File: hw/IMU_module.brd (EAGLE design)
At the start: 25 x 45 mm, 42 parts, among them J1 GROVE-4P-2.0-3470130P1, J2 GROVE-4P-2.0-3470130P1, X1 53047-06

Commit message: moved LSM303D interrupt lines
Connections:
- net AM_INT1: now also U$6.12; no longer U$6.11
- net AM_INT2: now also U$6.13; no longer U$6.12
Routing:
- net AM_INT2: track 4.09 -> 1.97 mm
- net AM_INT1: track 5.23 -> 3.68 mm
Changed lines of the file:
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@@
 </signal>
 <signal name="AM_INT1">
-<contactref element="U$6" pad="11"/>
 <contactref element="U$8" pad="P$11"/>
-<wire x1="18.5" y1="22.7" x2="18.5" y2="21.8" width="0.2" layer="1"/>
-<wire x1="18.5" y1="21.8" x2="19.9" y2="20.4" width="0.2" layer="1"/>
-<wire x1="19.9" y1="20.4" x2="19.9" y2="19" width="0.2" layer="1"/>
-<wire x1="19.9" y1="19" x2="19.7" y2="18.8" width="0.2" layer="1"/>
-<wire x1="19.05" y1="18.75" x2="19.65" y2="18.75" width="0.2" layer="1"/>
-<wire x1="19.65" y1="18.75" x2="19.7" y2="18.8" width="0.2" layer="1"/>
+<contactref element="U$6" pad="12"/>
+<wire x1="18.5" y1="22.7" x2="18.5" y2="21.9" width="0.2" layer="1"/>
+<wire x1="19.05" y1="19.25" x2="19.05" y2="21.35" width="0.2" layer="1"/>
+<wire x1="19.05" y1="21.35" x2="18.5" y2="21.9" width="0.2" layer="1"/>
 </signal>
 <signal name="AM_INT2">
-<contactref element="U$6" pad="12"/>
 <contactref element="U$8" pad="P$9"/>
-<wire x1="17.5" y1="22.7" x2="17.5" y2="22.2" width="0.2" layer="1"/>
-<wire x1="19.05" y1="19.25" x2="19.05" y2="20.65" width="0.2" layer="1"/>
-<wire x1="17.5" y1="22.2" x2="19.05" y2="20.65" width="0.2" layer="1"/>
+<contactref element="U$6" pad="13"/>
+<wire x1="17.55" y1="20.75" x2="17.55" y2="21.85" width="0.2" layer="1"/>
+<wire x1="17.55" y1="21.85" x2="17.5" y2="21.9" width="0.2" layer="1"/>
+<wire x1="17.5" y1="21.9" x2="17.5" y2="22.7" width="0.2" layer="1"/>
 </signal>
 <signal name="BAR_CS">

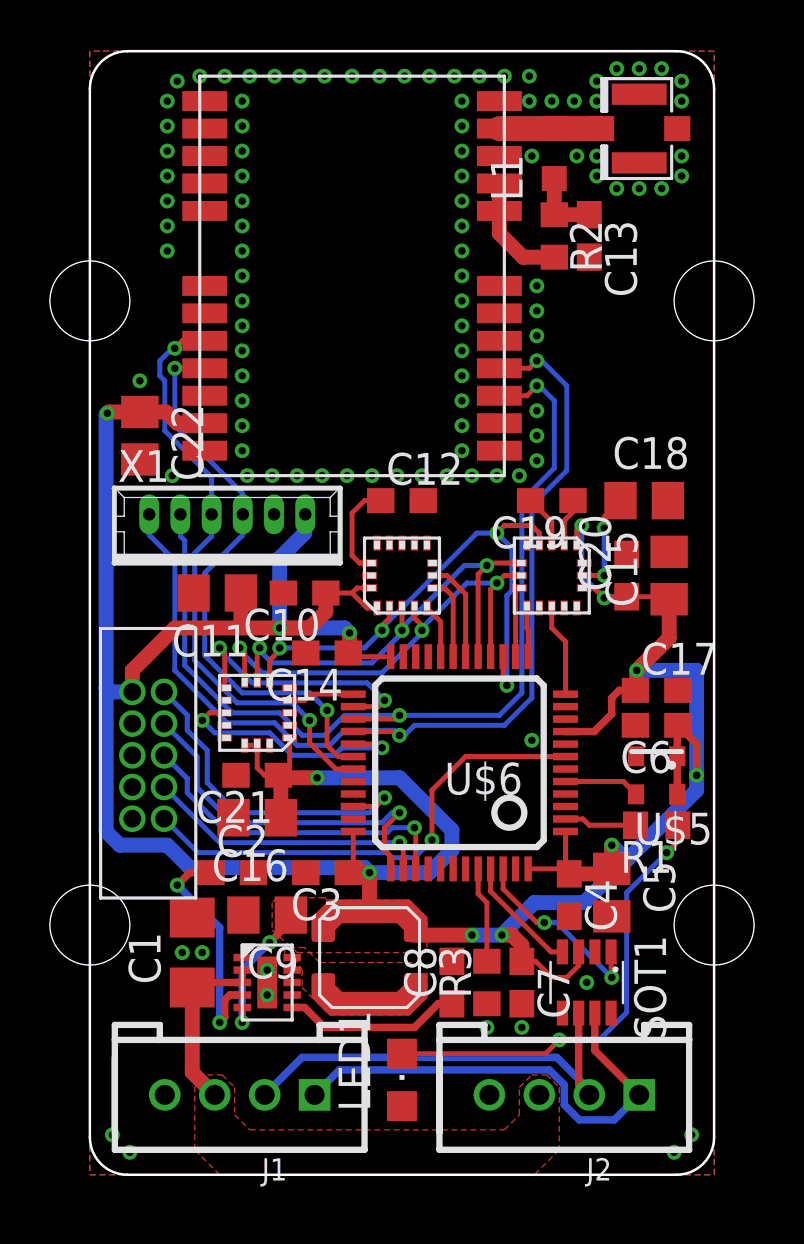
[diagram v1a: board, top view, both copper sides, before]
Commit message: approved DRC false errors
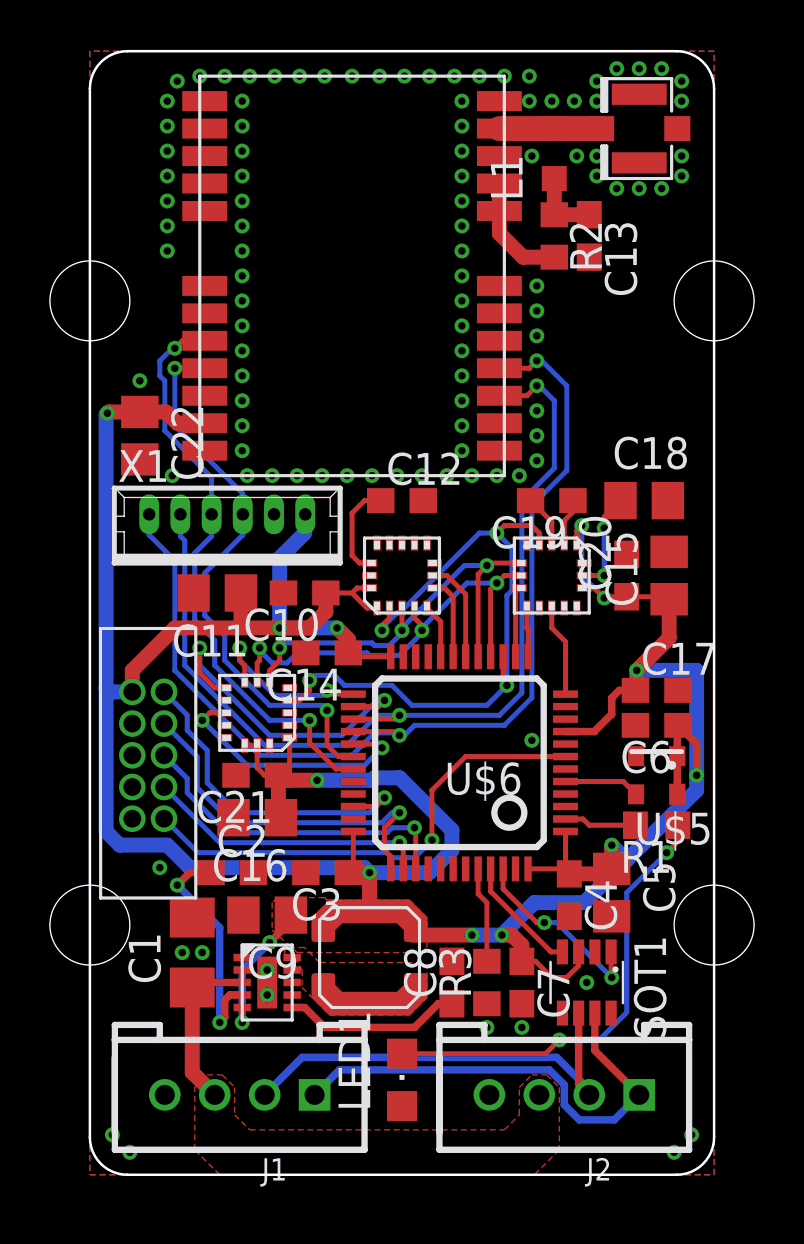
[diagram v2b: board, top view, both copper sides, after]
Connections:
- net BAR_CS: now also U$9.P$8; no longer U$9.P$4
- net MISO: now also U$9.P$7; no longer U$9.P$8
- net MOSI: now also U$9.P$6; no longer U$9.P$7
- net SCK: now also U$9.P$4; no longer U$9.P$6
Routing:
- net BAR_CS: track 2.65 -> 7.16 mm, vias 0 -> 2
- net SCK: track 23.1 -> 27.5 mm
- net BAR_INT2: track 10.6 -> 13.4 mm
- net MOSI: track 18.5 -> 17.4 mm
- net MISO: track 18.9 -> 17.8 mm
